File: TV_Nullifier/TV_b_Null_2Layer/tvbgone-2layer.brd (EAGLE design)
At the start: 18 x 42.4 mm, 18 parts, among them IC1 ATTINY85V-10S, Q1 BC857AT115, Q2 PMBT3904VS_DUAL_NPN, Y1_8MHZ RESONATOR

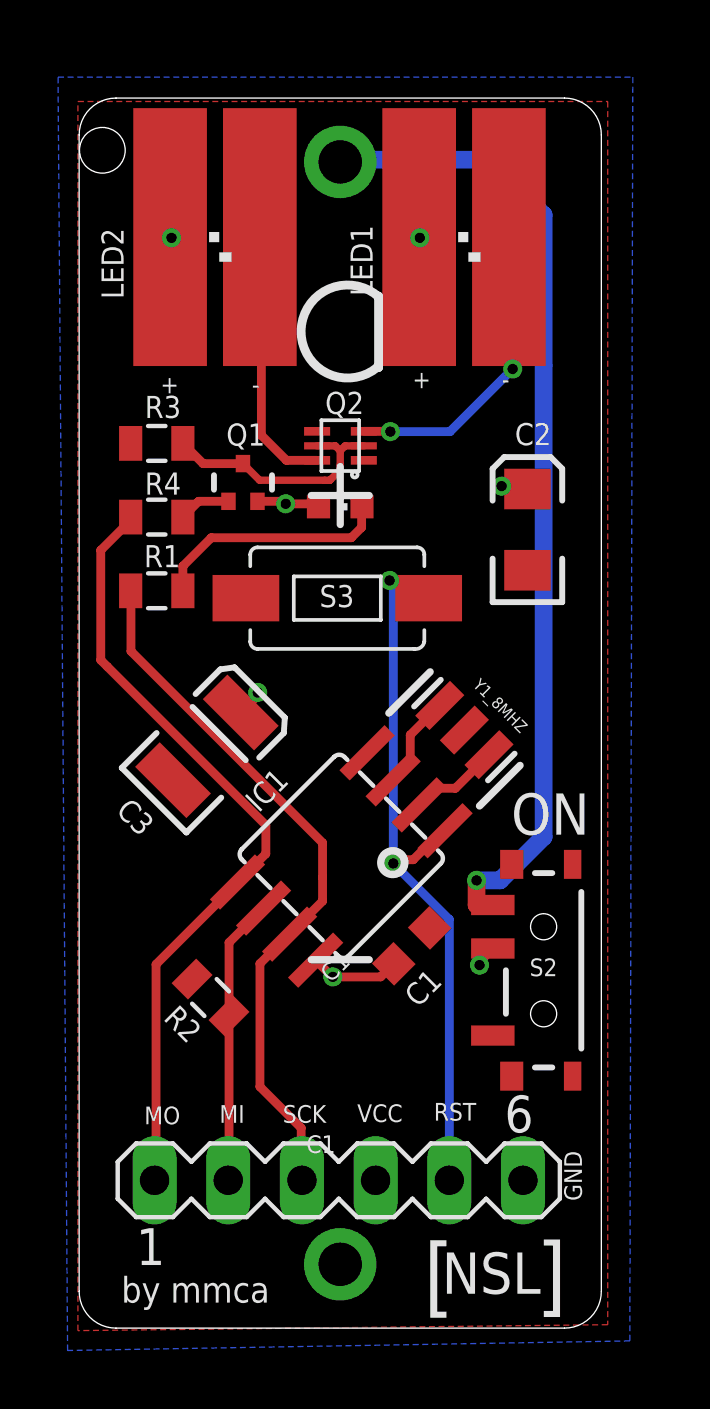
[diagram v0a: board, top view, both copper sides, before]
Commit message: 
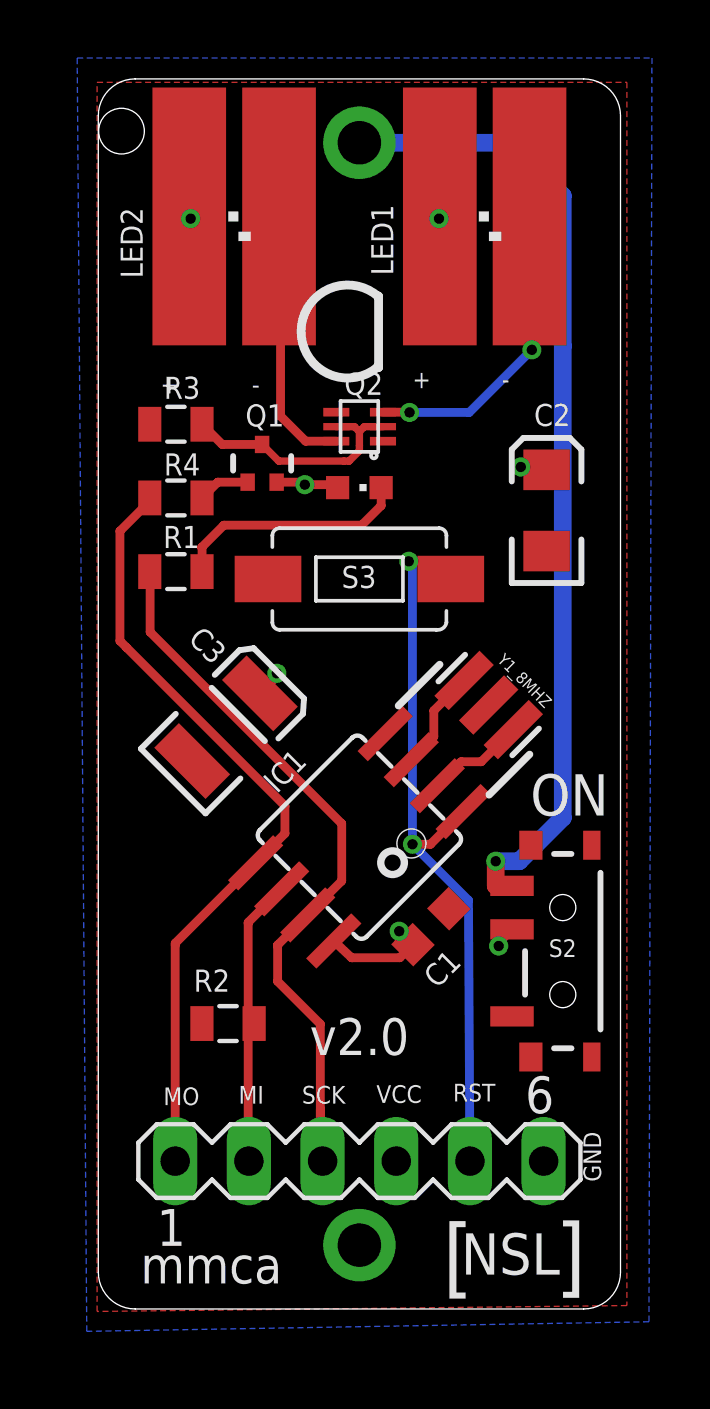
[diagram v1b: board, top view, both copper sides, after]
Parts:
- BAT1: device tvbgone-adj:BATTERY_CR123A -> tvbgone-2layer:TVBGONE-ADJ_BATTERY_CR123A
- Y1_8MHZ: device SparkFun:RESONATOR-SMD -> tvbgone-2layer:SPARKFUN_RESONATOR-SMD
- moved Y1_8MHZ 1.20 mm to (4.46, -0.38)
- moved R2 1.08 mm to (-4.53, -11.4), turned to 0 degrees
- moved S3 1.01 mm to (0.00, 3.96)
- moved LED1 1.01 mm to (4.32, 16.5)
- moved LED2 0.97 mm to (-4.32, 16.5)
- moved SV1 0.97 mm to (0.00, -16.1)
- moved Q2 0.93 mm to (0.00, 9.22)
- moved R3 0.93 mm to (-6.32, 9.30)
- moved S2 0.93 mm to (7.01, -8.86)
- moved Q1 0.93 mm to (-3.35, 7.95)
- moved C2 0.93 mm to (6.45, 6.32)
- moved R1 0.93 mm to (-6.32, 4.22)
- moved R4 0.93 mm to (-6.32, 6.76)
- moved BAT1 0.93 mm to (0.00, 0.00)
- moved LED3 0.93 mm to (0.00, 7.11)
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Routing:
- net SCK: track 24.6 -> 26.0 mm
- net VCC: track 13.1 -> 14.1 mm
- net MISO: track 11.2 -> 10.5 mm
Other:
- board text added: "mmca"
- board text added: "v2.0"
- board text removed: "C1"
- board text removed: "by mmca"

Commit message: 
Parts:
- R1: value 1.5K -> 10K
- R2: value 10K -> 1K
- R3: value 10K -> 1.5K
- R4: value 1K -> 10K
- moved R2 18.2 mm to (-6.32, 6.76), turned to 180 degrees
- moved R4 18.2 mm to (-4.53, -11.4), turned to 0 degrees
- moved R1 5.08 mm to (-6.32, 9.30), turned to 180 degrees
- moved R3 5.08 mm to (-6.32, 4.22), turned to 0 degrees
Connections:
- net GND: now also R1.2, R4.1; no longer R2.1, R3.2
- net MISO: now also R4.2; no longer R2.2
- net MOSI: now also R2.2; no longer R4.2
- net N$3: now also R3.2; no longer R1.2
- net N$6: now also R2.1; no longer R4.1
- net N$9: now also R1.1; no longer R3.1
- net SCK: now also R3.1; no longer R1.1
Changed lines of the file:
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@@
 <layer number="26" name="bNames" color="7" fill="1" visible="yes" active="yes"/>
 <layer number="27" name="tValues" color="7" fill="1" visible="no" active="yes"/>
-<layer number="28" name="bValues" color="7" fill="1" visible="no" active="yes"/>
+<layer number="28" name="bValues" color="7" fill="1" visible="yes" active="yes"/>
 <layer number="29" name="tStop" color="7" fill="3" visible="no" active="yes"/>
 <layer number="30" name="bStop" color="7" fill="6" visible="no" active="yes"/>
@@
 <attribute name="VALUE" x="-3.3528" y="7.874" size="0.635" layer="27" font="vector" rot="R270"/>
 </element>
-<element name="R1" library="SparkFun" package="0805" value="1.5K" x="-6.3246" y="4.2164" smashed="yes">
+<element name="R3" library="SparkFun" package="0805" value="1.5K" x="-6.3246" y="4.2164" smashed="yes">
 <attribute name="NAME" x="-5.5118" y="5.7912" size="0.762" layer="21" font="vector" rot="R180"/>
 <attribute name="VALUE" x="-7.0104" y="5.334" size="0.4064" layer="27"/>
 </element>
-<element name="R3" library="SparkFun" package="0805" value="10K" x="-6.3246" y="9.2964" smashed="yes" rot="R180">
+<element name="R1" library="SparkFun" package="0805" value="10K" x="-6.3246" y="9.2964" smashed="yes" rot="R180">
 <attribute name="NAME" x="-5.4864" y="10.9347" size="0.762" layer="21" font="vector" rot="R180"/>
 <attribute name="VALUE" x="-7.7978" y="8.0264" size="0.4064" layer="27"/>
 </element>
-<element name="R2" library="SparkFun" package="0805" value="10K" x="-4.5286375" y="-11.3612375" smashed="yes">
+<element name="R4" library="SparkFun" package="0805" value="10K" x="-4.5286375" y="-11.3612375" smashed="yes">
 <attribute name="NAME" x="-5.71245" y="-10.2633375" size="0.762" layer="21" font="vector"/>
 <attribute name="VALUE" x="-5.16364375" y="-9.761034375" size="0.508" layer="27" font="vector" rot="R180"/>
@@
 <attribute name="VALUE" x="-5.7912" y="13.9192" size="1.27" layer="27"/>
 </element>
-<element name="R4" library="SparkFun" package="0805" value="1K" x="-6.3246" y="6.7564" smashed="yes" rot="R180">
+<element name="R2" library="SparkFun" package="0805" value="1K" x="-6.3246" y="6.7564" smashed="yes" rot="R180">
 <attribute name="NAME" x="-5.4864" y="8.2931" size="0.762" layer="21" font="vector" rot="R180"/>
 <attribute name="VALUE" x="-5.3086" y="8.1534" size="0.4064" layer="27" rot="R180"/>
@@
 <contactref element="C1" pad="2"/>
 <contactref element="C2" pad="C"/>
-<contactref element="R2" pad="1"/>
+<contactref element="R4" pad="1"/>
 <contactref element="SV1" pad="6"/>
 <contactref element="Y1_8MHZ" pad="2"/>
 <contactref element="BAT1" pad="-"/>
-<contactref element="R3" pad="2"/>
+<contactref element="R1" pad="2"/>
 <polygon width="0.3048" layer="1">
 <vertex x="-9.0424" y="21.082"/>
@@
 <signal name="N$3">
 <contactref element="LED3" pad="C"/>
-<contactref element="R1" pad="2"/>
+<contactref element="R3" pad="2"/>
 <wire x1="0.7366" y1="7.0986" x2="0.75" y2="7.112" width="0.3048" layer="1"/>
 <wire x1="-5.4246" y1="4.2164" x2="-5.4246" y2="5.0546" width="0.3048" layer="1"/>
@@
 <contactref element="SV1" pad="1"/>
 <contactref element="IC1" pad="5"/>
-<contactref element="R4" pad="2"/>
+<contactref element="R2" pad="2"/>
 <wire x1="-3.577253125" y1="-5.821275" x2="-3.541253125" y2="-5.852653125" width="0.3048" layer="1"/>
 <wire x1="-6.35" y1="-8.6614" x2="-6.35" y2="-16.0528" width="0.3048" layer="1"/>
@@
 <contactref element="SV1" pad="2"/>
 <contactref element="IC1" pad="6"/>
-<contactref element="R2" pad="2"/>
+<contactref element="R4" pad="2"/>
 <wire x1="-3.834003125" y1="-7.910078125" x2="-3.834003125" y2="-10.8966" width="0.3048" layer="1"/>
 <wire x1="-3.834003125" y1="-10.8966" x2="-3.834003125" y2="-11.3612375" width="0.3048" layer="1"/>
@@
 <contactref element="SV1" pad="3"/>
 <contactref element="IC1" pad="7"/>
-<contactref element="R1" pad="1"/>
+<contactref element="R3" pad="1"/>
 <wire x1="-1.7812" y1="-7.617325" x2="-1.749925" y2="-7.617325" width="0.3048" layer="1"/>
 <wire x1="-1.3462" y1="-14.3002" x2="-1.3462" y2="-15.5956" width="0.3048" layer="1"/>
@@
 <signal name="N$6">
 <contactref element="Q1" pad="2"/>
-<contactref element="R4" pad="1"/>
+<contactref element="R2" pad="1"/>
 <wire x1="-5.4246" y1="6.7564" x2="-4.8808" y2="7.3002" width="0.3048" layer="1"/>
 <wire x1="-4.8808" y1="7.3002" x2="-3.8528" y2="7.3002" width="0.3048" layer="1"/>
@@
 <signal name="N$9">
 <contactref element="Q1" pad="1"/>
-<contactref element="R3" pad="1"/>
+<contactref element="R1" pad="1"/>
 <contactref element="Q2" pad="2"/>
 <contactref element="Q2" pad="5"/>

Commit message: 
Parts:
- LED1, LED2: device tvbgone3:SIDE_IR_NSL@1 -> tvbgone-2layer:TVBGONE3_SIDE_IR_NSL
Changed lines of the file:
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@@
 <?xml version="1.0" encoding="utf-8"?>
 <!DOCTYPE eagle SYSTEM "eagle.dtd">
-<eagle version="6.4">
+<eagle version="6.5.0">
 <drawing>
 <settings>
@@
 <attribute name="VALUE" x="-2.5908" y="8.5598" size="0.508" layer="27" font="vector"/>
 </element>
-<element name="LED1" library="tvbgone3" package="SIDE_IR_NSL@1" value="" x="4.318" y="16.4592" smashed="yes">
+<element name="LED1" library="tvbgone-2layer" package="TVBGONE3_SIDE_IR_NSL" value="" x="4.318" y="16.4592" smashed="yes">
 <attribute name="NAME" x="1.1684" y="14.4272" size="0.762" layer="25" font="vector" rot="R90"/>
 <attribute name="VALUE" x="6.858" y="14.986" size="1.27" layer="27" rot="R90"/>
 </element>
-<element name="LED2" library="tvbgone3" package="SIDE_IR_NSL@1" value="" x="-4.318" y="16.4592" smashed="yes">
+<element name="LED2" library="tvbgone-2layer" package="TVBGONE3_SIDE_IR_NSL" value="" x="-4.318" y="16.4592" smashed="yes">
 <attribute name="NAME" x="-7.4676" y="14.3256" size="0.762" layer="25" font="vector" rot="R90"/>
 <attribute name="VALUE" x="-5.7912" y="13.9192" size="1.27" layer="27"/>

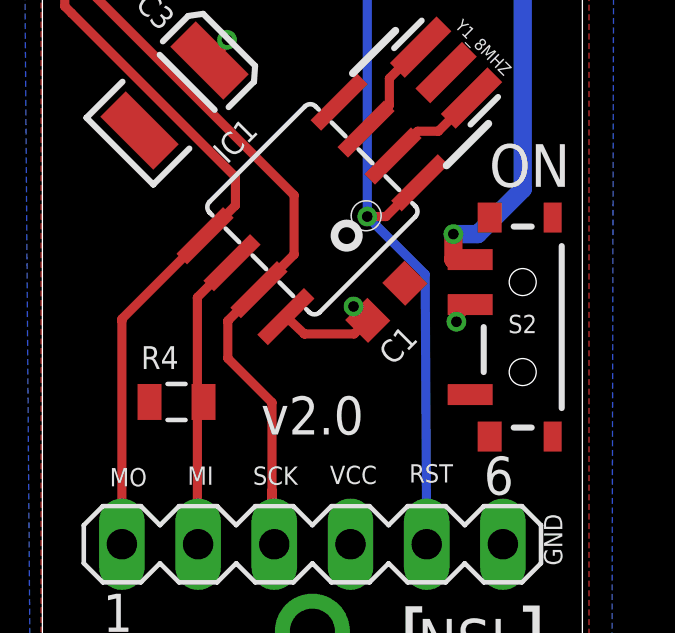
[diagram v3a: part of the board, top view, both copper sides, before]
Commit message: 
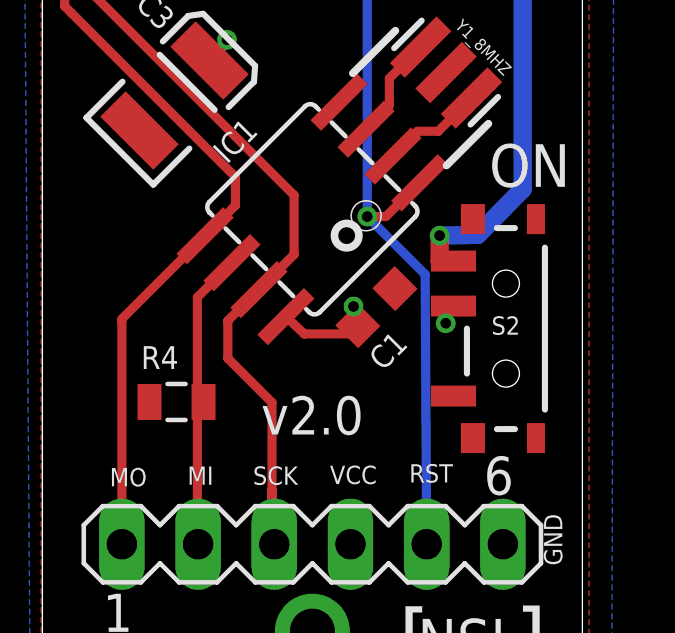
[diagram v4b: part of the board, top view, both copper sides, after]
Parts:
- moved S2 0.56 mm to (6.45, -8.92)
- moved C1 0.38 mm to (2.13, -8.20)
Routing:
- net VCC: track 14.1 -> 13.4 mm

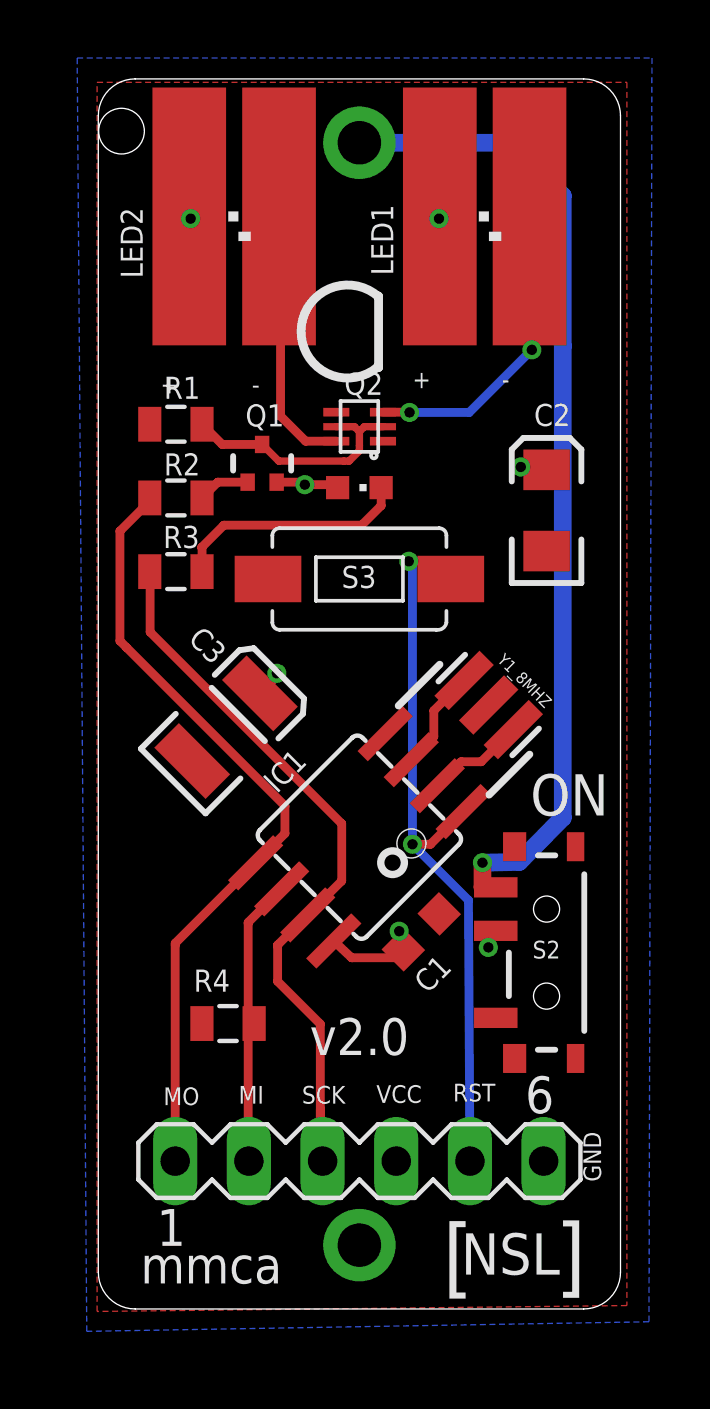
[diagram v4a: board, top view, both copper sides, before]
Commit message: 
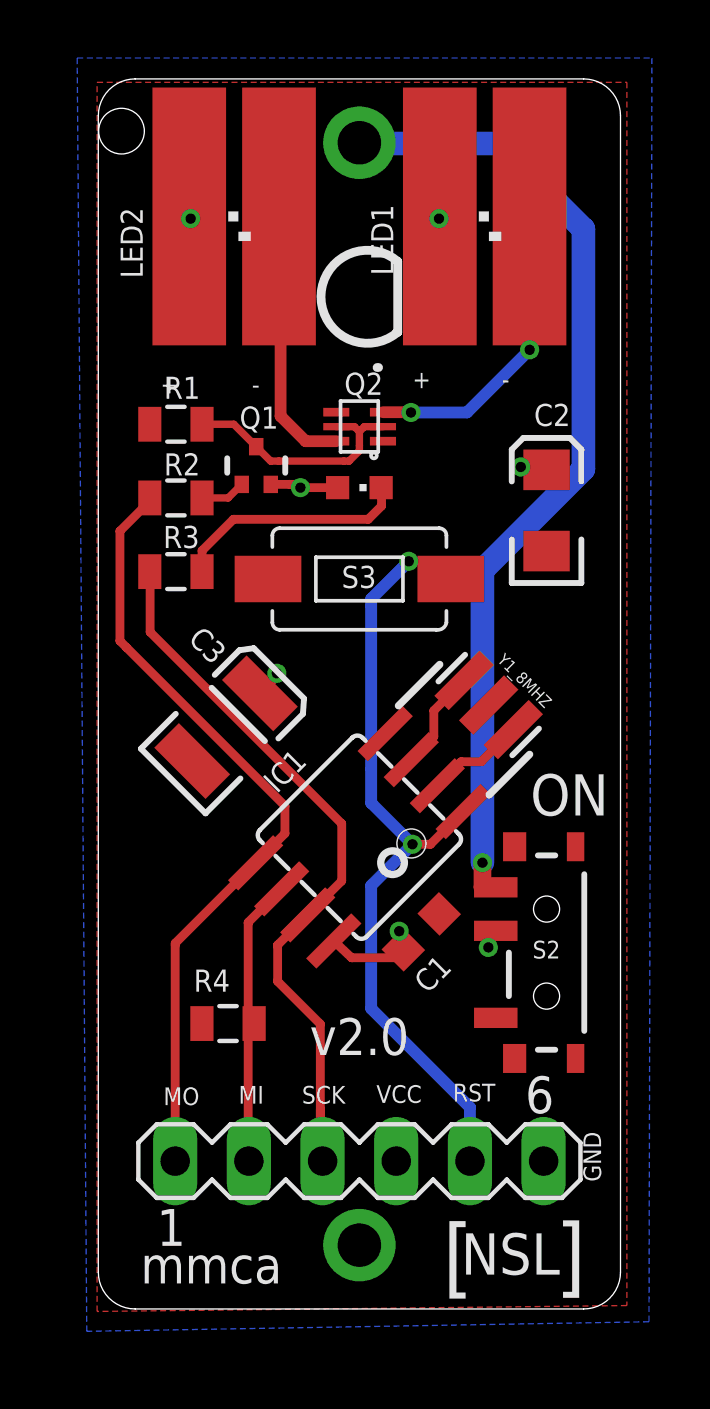
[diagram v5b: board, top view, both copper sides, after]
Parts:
- moved Q1 0.22 mm to (-3.56, 7.87)
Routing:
- net RST: track 25.8 -> 28.1 mm
